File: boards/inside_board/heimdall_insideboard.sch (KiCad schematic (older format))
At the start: 53 parts, among them J1 Barrel_Jack_Switch, J2 Screw_Terminal_01x04, J3 Conn_01x09, J4 Screw_Terminal_01x04, J5 Conn_01x09, J6 Screw_Terminal_01x04, J7 Screw_Terminal_01x06, J8 Screw_Terminal_01x09, J9 Screw_Terminal_01x02, K1 Relay_HJR-3FF-S-Z-5VDC, K2 Relay_HJR-3FF-S-Z-5VDC, K3 Relay_HJR-3FF-S-Z-5VDC, Q1 2N3904, Q2 2N3904, Q3 2N3904, Q4 2N3904, Q5 2N3904, U1 LM1117-3.3, U2 L7805, U3 ESP32_Dev_Board_30Pin

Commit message: update the inside board PCB design file
a number of changes:

 - add an extra terminal to the wiegand header for the 26/34 mode
   switching pin that most wiegand readers have, complete with a
   jumper to selectively connect that terminal to ground
 - expand screw terminal silkscreen outline to fit the actual size
   of the screw terminals; i misread the datasheet when laying them
   out in the previous board revision
 - move the 5v regulator .2" to the right so that there's more
   clearance between it and the 3.3v one when the heatsinks are
   attached
 - correspondingly, move the ESP32 left by about .1" to make room
   for the tamper switch screw terminal's actual size
 - move neighboring resistors closer since they fit well within
   their component outline
 - change the transistor footprint to one with wider spacing, for
   ease of soldering by volunteers
 - add labels for the 12v plug and the fuse that can still be seen
   once the components are installed
 - add a through-hole addressable RGB LED for board status
   signalling and other shenanigans
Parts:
- added D4: NeoPixel_THT, LED_THT:LED_D5.0mm-4_RGB_Wide_Pins, symbol LED:NeoPixel_THT
- added JP4: Jumper, Connector_PinHeader_2.54mm:PinHeader_1x02_P2.54mm_Vertical, symbol Jumper:Jumper_2_Open
- J7: footprint Javawizard_Common_Footprints:PinHeader_JW_1x06_P5.00mm_Vertical -> Javawizard_Common_Footprints:PinHeader_JW_1x07_P5.00mm_Vertical; symbol Connector:Screw_Terminal_01x06 -> Connector:Screw_Terminal_01x07
- K1, K2, K3: symbol Javawizard_Common_Schematic_Symbols:Relay_HJR-3FF-S-Z-5VDC -> heimdall_insideboard-rescue:Relay_HJR-3FF-S-Z-5VDC-Javawizard_Common_Schematic_Symbols
- Q1, Q2, Q3, Q4, Q5: footprint Package_TO_SOT_THT:TO-92_Inline -> Package_TO_SOT_THT:TO-92_Inline_Wide
- U3: symbol Javawizard_Common_Schematic_Symbols:ESP32_Dev_Board_30Pin -> heimdall_insideboard-rescue:ESP32_Dev_Board_30Pin-Javawizard_Common_Schematic_Symbols
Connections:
- net +12V: now also J7.7 (Pin_7); no longer J7.6 (Pin_6)
- net +5V: now also D4.3 (VDD)
- net GND: now also J2.1 (Pin_1), J4.1 (Pin_1), J6.1 (Pin_1), J7.6 (Pin_6), D4.2 (GND), JP4.1 (A); no longer J2.4 (Pin_4), J4.4 (Pin_4), J6.4 (Pin_4), J7.5 (Pin_5)
- net RELAY1_C: now also J2.3 (Pin_3); no longer J2.2 (Pin_2)
- net RELAY1_NC: now also J2.4 (Pin_4); no longer J2.1 (Pin_1)
- net RELAY1_NO: now also J2.2 (Pin_2); no longer J2.3 (Pin_3)
- net RELAY2_C: now also J4.3 (Pin_3); no longer J4.2 (Pin_2)
- net RELAY2_NC: now also J4.4 (Pin_4); no longer J4.1 (Pin_1)
- net RELAY2_NO: now also J4.2 (Pin_2); no longer J4.3 (Pin_3)
- net RELAY3_C: now also J6.3 (Pin_3); no longer J6.2 (Pin_2)
- net RELAY3_NC: now also J6.4 (Pin_4); no longer J6.1 (Pin_1)
- net RELAY3_NO: now also J6.2 (Pin_2); no longer J6.3 (Pin_3)
- net at U3.18 (IO15_PWM): now also D4.4 (DIN)
- new net: J7.5 (Pin_5), JP4.2 (B)
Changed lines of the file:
@@
 $EndComp
 $Comp
-L Javawizard_Common_Schematic_Symbols:ESP32_Dev_Board_30Pin U3
+L heimdall_insideboard-rescue:ESP32_Dev_Board_30Pin-Javawizard_Common_Schematic_Symbols U3
 U 1 1 5F0E43E4
 P 5200 3000
@@
 	4350 4550 4400 4550
 $Comp
-L Javawizard_Common_Schematic_Symbols:Relay_HJR-3FF-S-Z-5VDC K1
+L heimdall_insideboard-rescue:Relay_HJR-3FF-S-Z-5VDC-Javawizard_Common_Schematic_Symbols K1
 U 1 1 5F0E96C1
 P 8800 650
@@
 F 0 "Q1" H 8640 1846 50  0000 L CNN
 F 1 "2N3904" H 8640 1755 50  0000 L CNN
-F 2 "Package_TO_SOT_THT:TO-92_Inline" H 8650 1725 50  0001 L CIN
+F 2 "Package_TO_SOT_THT:TO-92_Inline_Wide" H 8650 1725 50  0001 L CIN
 F 3 "https://www.fairchildsemi.com/datasheets/2N/2N3904.pdf" H 8450 1800 50  0001 L CNN
 	1    8450 1800
@@
 L Connector:Screw_Terminal_01x04 J2
 U 1 1 5F123CCA
-P 10200 1900
-F 0 "J2" H 10280 1892 50  0000 L CNN
-F 1 "Screw_Terminal_01x04" H 10280 1801 50  0000 L CNN
-F 2 "Javawizard_Common_Footprints:PinHeader_JW_1x04_P5.00mm_Vertical" H 10200 1900 50  0001 C CNN
-F 3 "~" H 10200 1900 50  0001 C CNN
-	1    10200 1900
-	1    0    0    -1
+P 10200 2000
+F 0 "J2" H 10280 1992 50  0000 L CNN
+F 1 "Screw_Terminal_01x04" H 10280 1901 50  0000 L CNN
+F 2 "Javawizard_Common_Footprints:PinHeader_JW_1x04_P5.00mm_Vertical" H 10200 2000 50  0001 C CNN
+F 3 "~" H 10200 2000 50  0001 C CNN
+	1    10200 2000
+	1    0    0    1
 $EndComp
 Wire Wire Line
@@
 	7450 4050 7450 3700
 $Comp
-L Javawizard_Common_Schematic_Symbols:Relay_HJR-3FF-S-Z-5VDC K2
+L heimdall_insideboard-rescue:Relay_HJR-3FF-S-Z-5VDC-Javawizard_Common_Schematic_Symbols K2
 U 1 1 5F14E304
 P 8800 2550
@@
 F 0 "Q2" H 8640 3746 50  0000 L CNN
 F 1 "2N3904" H 8640 3655 50  0000 L CNN
-F 2 "Package_TO_SOT_THT:TO-92_Inline" H 8650 3625 50  0001 L CIN
+F 2 "Package_TO_SOT_THT:TO-92_Inline_Wide" H 8650 3625 50  0001 L CIN
 F 3 "https://www.fairchildsemi.com/datasheets/2N/2N3904.pdf" H 8450 3700 50  0001 L CNN
 	1    8450 3700
@@
 L Connector:Screw_Terminal_01x04 J4
 U 1 1 5F14E335
-P 10200 3800
-F 0 "J4" H 10280 3792 50  0000 L CNN
-F 1 "Screw_Terminal_01x04" H 10280 3701 50  0000 L CNN
-F 2 "Javawizard_Common_Footprints:PinHeader_JW_1x04_P5.00mm_Vertical" H 10200 3800 50  0001 C CNN
-F 3 "~" H 10200 3800 50  0001 C CNN
-	1    10200 3800
-	1    0    0    -1
+P 10200 3900
+F 0 "J4" H 10280 3892 50  0000 L CNN
+F 1 "Screw_Terminal_01x04" H 10280 3801 50  0000 L CNN
+F 2 "Javawizard_Common_Footprints:PinHeader_JW_1x04_P5.00mm_Vertical" H 10200 3900 50  0001 C CNN
+F 3 "~" H 10200 3900 50  0001 C CNN
+	1    10200 3900
+	1    0    0    1
 $EndComp
 Wire Wire Line
@@
 	10500 2750 10500 2850
 $Comp
-L Javawizard_Common_Schematic_Symbols:Relay_HJR-3FF-S-Z-5VDC K3
+L heimdall_insideboard-rescue:Relay_HJR-3FF-S-Z-5VDC-Javawizard_Common_Schematic_Symbols K3
 U 1 1 5F1565E6
 P 8800 4450
@@
 F 0 "Q3" H 8640 5646 50  0000 L CNN
 F 1 "2N3904" H 8640 5555 50  0000 L CNN
-F 2 "Package_TO_SOT_THT:TO-92_Inline" H 8650 5525 50  0001 L CIN
+F 2 "Package_TO_SOT_THT:TO-92_Inline_Wide" H 8650 5525 50  0001 L CIN
 F 3 "https://www.fairchildsemi.com/datasheets/2N/2N3904.pdf" H 8450 5600 50  0001 L CNN
 	1    8450 5600
@@
 L Connector:Screw_Terminal_01x04 J6
 U 1 1 5F156617
-P 10200 5700
-F 0 "J6" H 10280 5692 50  0000 L CNN
-F 1 "Screw_Terminal_01x04" H 10280 5601 50  0000 L CNN
-F 2 "Javawizard_Common_Footprints:PinHeader_JW_1x04_P5.00mm_Vertical" H 10200 5700 50  0001 C CNN
-F 3 "~" H 10200 5700 50  0001 C CNN
-	1    10200 5700
-	1    0    0    -1
+P 10200 5800
+F 0 "J6" H 10280 5792 50  0000 L CNN
+F 1 "Screw_Terminal_01x04" H 10280 5701 50  0000 L CNN
+F 2 "Javawizard_Common_Footprints:PinHeader_JW_1x04_P5.00mm_Vertical" H 10200 5800 50  0001 C CNN
+F 3 "~" H 10200 5800 50  0001 C CNN
+	1    10200 5800
+	1    0    0    1
 $EndComp
 Wire Wire Line
@@
 	4100 3650 4400 3650
 $Comp
-L Connector:Screw_Terminal_01x06 J7
+L Connector:Screw_Terminal_01x07 J7
 U 1 1 5F2A191F
-P 1250 6150
-F 0 "J7" H 1168 5625 50  0000 C CNN
-F 1 "Screw_Terminal_01x06" H 1168 5716 50  0000 C CNN
-F 2 "Javawizard_Common_Footprints:PinHeader_JW_1x06_P5.00mm_Vertical" H 1250 6150 50  0001 C CNN
-F 3 "~" H 1250 6150 50  0001 C CNN
-	1    1250 6150
+P 1250 6050
+F 0 "J7" H 1168 5525 50  0000 C CNN
+F 1 "Screw_Terminal_01x06" H 1168 5616 50  0000 C CNN
+F 2 "Javawizard_Common_Footprints:PinHeader_JW_1x07_P5.00mm_Vertical" H 1250 6050 50  0001 C CNN
+F 3 "~" H 1250 6050 50  0001 C CNN
+	1    1250 6050
 	-1   0    0    1
 $EndComp
@@
 L power:+12V #PWR022
 U 1 1 5F2A5516
-P 2000 5650
-F 0 "#PWR022" H 2000 5500 50  0001 C CNN
-F 1 "+12V" H 2015 5823 50  0000 C CNN
-F 2 "" H 2000 5650 50  0001 C CNN
-F 3 "" H 2000 5650 50  0001 C CNN
-	1    2000 5650
-	1    0    0    -1
-$EndComp
-Wire Wire Line
-	2000 5850 1450 5850
+P 2000 5550
+F 0 "#PWR022" H 2000 5400 50  0001 C CNN
+F 1 "+12V" H 2015 5723 50  0000 C CNN
+F 2 "" H 2000 5550 50  0001 C CNN
+F 3 "" H 2000 5550 50  0001 C CNN
+	1    2000 5550
+	1    0    0    -1
+$EndComp
+Wire Wire Line
+	2000 5750 1450 5750
 $Comp
 L power:GND #PWR028
 U 1 1 5F2ADB21
-P 2000 6650
-F 0 "#PWR028" H 2000 6400 50  0001 C CNN
-F 1 "GND" H 2005 6477 50  0000 C CNN
-F 2 "" H 2000 6650 50  0001 C CNN
-F 3 "" H 2000 6650 50  0001 C CNN
-	1    2000 6650
-	1    0    0    -1
-$EndComp
-Wire Wire Line
-	2000 6650 2000 5950
-Wire Wire Line
-	2000 5950 1450 5950
+P 2000 7200
+F 0 "#PWR028" H 2000 6950 50  0001 C CNN
+F 1 "GND" H 2005 7027 50  0000 C CNN
+F 2 "" H 2000 7200 50  0001 C CNN
+F 3 "" H 2000 7200 50  0001 C CNN
+	1    2000 7200
+	1    0    0    -1
+$EndComp
+Wire Wire Line
+	2000 5850 1450 5850
 $Comp
 L Device:R_Small_US R16
@@
 $EndComp
 Wire Wire Line
-	2000 5850 2000 5650
+	2000 5750 2000 5550
 $Comp
 L Device:R_Small_US R22
@@
 F 0 "Q4" H 4140 7096 50  0000 L CNN
 F 1 "2N3904" H 4140 7005 50  0000 L CNN
-F 2 "Package_TO_SOT_THT:TO-92_Inline" H 4150 6975 50  0001 L CIN
+F 2 "Package_TO_SOT_THT:TO-92_Inline_Wide" H 4150 6975 50  0001 L CIN
 F 3 "https://www.fairchildsemi.com/datasheets/2N/2N3904.pdf" H 3950 7050 50  0001 L CNN
 	1    3950 7050
@@
 F 0 "Q5" H 4990 7096 50  0000 L CNN
 F 1 "2N3904" H 4990 7005 50  0000 L CNN
-F 2 "Package_TO_SOT_THT:TO-92_Inline" H 5000 6975 50  0001 L CIN
+F 2 "Package_TO_SOT_THT:TO-92_Inline_Wide" H 5000 6975 50  0001 L CIN
 F 3 "https://www.fairchildsemi.com/datasheets/2N/2N3904.pdf" H 4800 7050 50  0001 L CNN
 	1    4800 7050
@@
 Wire Wire Line
 	7000 3750 6000 3750
+$Comp
+L LED:NeoPixel_THT D4
+U 1 1 6058485B
+P 5350 5450
+F 0 "D4" H 5694 5496 50  0000 L CNN
+F 1 "NeoPixel_THT" H 5694 5405 50  0000 L CNN
+F 2 "LED_THT:LED_D5.0mm-4_RGB_Wide_Pins" H 5400 5150 50  0001 L TNN
+F 3 "https://www.adafruit.com/product/1938" H 5450 5075 50  0001 L TNN
+	1    5350 5450
+	1    0    0    -1
+$EndComp
+$Comp
+L power:+5V #PWR0104
+U 1 1 605868AC
+P 5350 5050
+F 0 "#PWR0104" H 5350 4900 50  0001 C CNN
+F 1 "+5V" H 5365 5223 50  0000 C CNN
+F 2 "" H 5350 5050 50  0001 C CNN
+F 3 "" H 5350 5050 50  0001 C CNN
+	1    5350 5050
+	1    0    0    -1
+$EndComp
+$Comp
+L power:GND #PWR0105
+U 1 1 605DA8FD
+P 5350 5950
+F 0 "#PWR0105" H 5350 5700 50  0001 C CNN
+F 1 "GND" H 5355 5777 50  0000 C CNN
+F 2 "" H 5350 5950 50  0001 C CNN
+F 3 "" H 5350 5950 50  0001 C CNN
+	1    5350 5950
+	1    0    0    -1
+$EndComp
+Wire Wire Line
+	5350 5050 5350 5150
+Wire Wire Line
+	5350 5750 5350 5950
+Wire Wire Line
+	6000 4350 6500 4350
+Wire Wire Line
+	6500 4350 6500 4800
+Wire Wire Line
+	6500 4800 4750 4800
+Wire Wire Line
+	4750 4800 4750 5450
+Wire Wire Line
+	4750 5450 5050 5450
+$Comp
+L Jumper:Jumper_2_Open JP4
+U 1 1 60618C40
+P 1600 6800
+F 0 "JP4" V 1646 6712 50  0000 R CNN
+F 1 "Jumper" V 1555 6712 50  0000 R CNN
+F 2 "Connector_PinHeader_2.54mm:PinHeader_1x02_P2.54mm_Vertical" H 1600 6800 50  0001 C CNN
+F 3 "~" H 1600 6800 50  0001 C CNN
+	1    1600 6800
+	0    -1   -1   0
+$EndComp
+Wire Wire Line
+	2000 5850 2000 7000
+Wire Wire Line
+	1600 6600 1600 5950
+Wire Wire Line
+	1600 5950 1450 5950
+Wire Wire Line
+	1600 7000 2000 7000
+Connection ~ 2000 7000
+Wire Wire Line
+	2000 7000 2000 7200
 $EndSCHEMATC

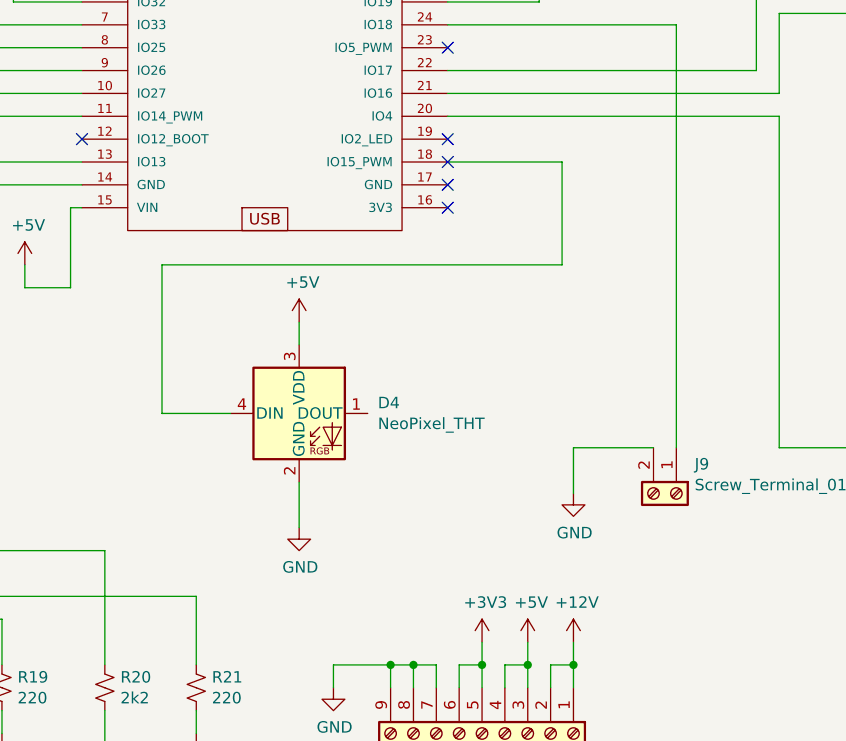
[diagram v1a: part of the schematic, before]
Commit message: inside board version 3
- add a 3.3v -> 5v level shifting circuit to the addressable RGB
  LED's input. it seems to work without it in my testing of board
  version 2, but I'd rather not find out the hard way that it works
  for some LEDs but not for others since it's out of spec for what
  they're supposed to require, which is 0.7*VCC = 3.5v for logic
  level high signals.
- a handful of vias were underneath where the voltage regulator
  heat sinks go. to prevent the heatsinks from coming in contact
  with them, move them outside of the heat sinks' footprint.
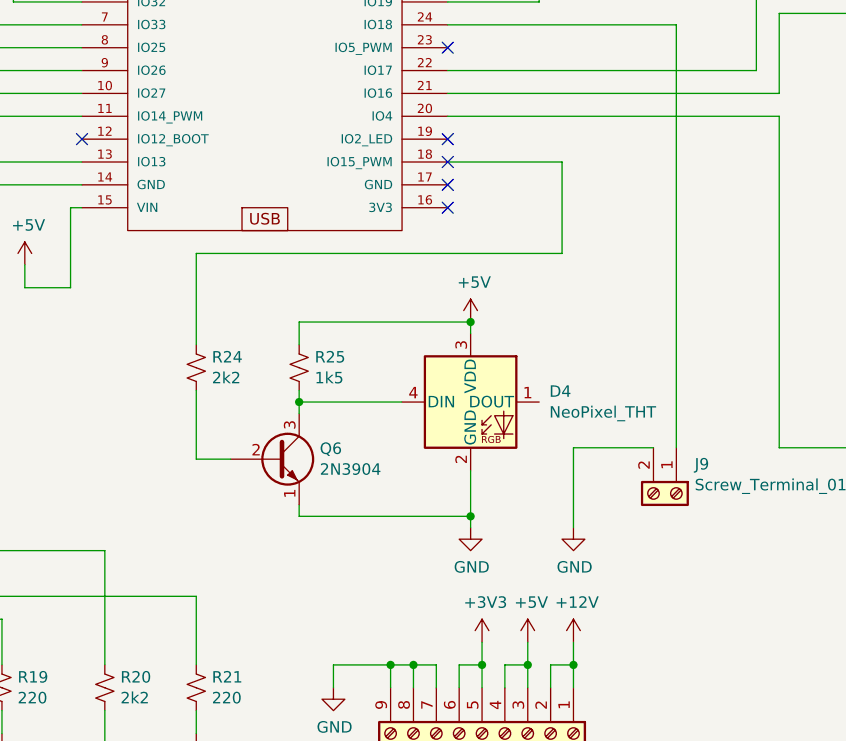
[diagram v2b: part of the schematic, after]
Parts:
- added Q6: 2N3904, Package_TO_SOT_THT:TO-92_Inline_Wide, symbol Transistor_BJT:2N3904
- added R24: 2k2, Resistor_THT:R_Axial_DIN0207_L6.3mm_D2.5mm_P10.16mm_Horizontal, symbol Device:R_Small_US
- added R25: 1k5, Resistor_THT:R_Axial_DIN0207_L6.3mm_D2.5mm_P10.16mm_Horizontal, symbol Device:R_Small_US
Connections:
- net +5V: now also R25.1
- net GND: now also Q6.1 (E)
- net at U3.18 (IO15_PWM): now also R24.1; no longer D4.4 (DIN)
- new net: D4.4 (DIN), Q6.3 (C), R25.2
- new net: Q6.2 (B), R24.2
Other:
- moved on the sheet: D4
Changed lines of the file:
@@
 L power:GND #PWR0103
 U 1 1 5F140007
-P 6550 5800
-F 0 "#PWR0103" H 6550 5550 50  0001 C CNN
-F 1 "GND" H 6555 5627 50  0000 C CNN
-F 2 "" H 6550 5800 50  0001 C CNN
-F 3 "" H 6550 5800 50  0001 C CNN
-	1    6550 5800
+P 6550 5950
+F 0 "#PWR0103" H 6550 5700 50  0001 C CNN
+F 1 "GND" H 6555 5777 50  0000 C CNN
+F 2 "" H 6550 5950 50  0001 C CNN
+F 3 "" H 6550 5950 50  0001 C CNN
+	1    6550 5950
 	1    0    0    -1
 $EndComp
 Wire Wire Line
 	6900 5600 6550 5600
-Wire Wire Line
-	6550 5600 6550 5800
 Wire Wire Line
 	7000 5600 7000 3750
@@
 L LED:NeoPixel_THT D4
 U 1 1 6058485B
-P 5350 5450
-F 0 "D4" H 5694 5496 50  0000 L CNN
-F 1 "NeoPixel_THT" H 5694 5405 50  0000 L CNN
-F 2 "LED_THT:LED_D5.0mm-4_RGB_Wide_Pins" H 5400 5150 50  0001 L TNN
-F 3 "https://www.adafruit.com/product/1938" H 5450 5075 50  0001 L TNN
-	1    5350 5450
+P 6100 5400
+F 0 "D4" H 6444 5446 50  0000 L CNN
+F 1 "NeoPixel_THT" H 6444 5355 50  0000 L CNN
+F 2 "LED_THT:LED_D5.0mm-4_RGB_Wide_Pins" H 6150 5100 50  0001 L TNN
+F 3 "https://www.adafruit.com/product/1938" H 6200 5025 50  0001 L TNN
+	1    6100 5400
 	1    0    0    -1
 $EndComp
@@
 L power:+5V #PWR0104
 U 1 1 605868AC
-P 5350 5050
-F 0 "#PWR0104" H 5350 4900 50  0001 C CNN
-F 1 "+5V" H 5365 5223 50  0000 C CNN
-F 2 "" H 5350 5050 50  0001 C CNN
-F 3 "" H 5350 5050 50  0001 C CNN
-	1    5350 5050
+P 6100 5050
+F 0 "#PWR0104" H 6100 4900 50  0001 C CNN
+F 1 "+5V" H 6115 5223 50  0000 C CNN
+F 2 "" H 6100 5050 50  0001 C CNN
+F 3 "" H 6100 5050 50  0001 C CNN
+	1    6100 5050
 	1    0    0    -1
 $EndComp
@@
 L power:GND #PWR0105
 U 1 1 605DA8FD
-P 5350 5950
-F 0 "#PWR0105" H 5350 5700 50  0001 C CNN
-F 1 "GND" H 5355 5777 50  0000 C CNN
-F 2 "" H 5350 5950 50  0001 C CNN
-F 3 "" H 5350 5950 50  0001 C CNN
-	1    5350 5950
+P 6100 5950
+F 0 "#PWR0105" H 6100 5700 50  0001 C CNN
+F 1 "GND" H 6105 5777 50  0000 C CNN
+F 2 "" H 6100 5950 50  0001 C CNN
+F 3 "" H 6100 5950 50  0001 C CNN
+	1    6100 5950
 	1    0    0    -1
 $EndComp
 Wire Wire Line
-	5350 5050 5350 5150
-Wire Wire Line
-	5350 5750 5350 5950
-Wire Wire Line
 	6000 4350 6500 4350
-Wire Wire Line
-	6500 4350 6500 4800
-Wire Wire Line
-	6500 4800 4750 4800
-Wire Wire Line
-	4750 4800 4750 5450
-Wire Wire Line
-	4750 5450 5050 5450
 $Comp
 L Jumper:Jumper_2_Open JP4
@@
 Wire Wire Line
 	2000 7000 2000 7200
+Wire Wire Line
+	6100 5100 6100 5050
+$Comp
+L Transistor_BJT:2N3904 Q6
+U 1 1 607CCCEB
+P 5250 5650
+F 0 "Q6" H 5440 5696 50  0000 L CNN
+F 1 "2N3904" H 5440 5605 50  0000 L CNN
+F 2 "Package_TO_SOT_THT:TO-92_Inline_Wide" H 5450 5575 50  0001 L CIN
+F 3 "https://www.fairchildsemi.com/datasheets/2N/2N3904.pdf" H 5250 5650 50  0001 L CNN
+	1    5250 5650
+	1    0    0    -1
+$EndComp
+$Comp
+L Device:R_Small_US R25
+U 1 1 607CE114
+P 5350 5250
+F 0 "R25" H 5418 5296 50  0000 L CNN
+F 1 "1k5" H 5418 5205 50  0000 L CNN
+F 2 "Resistor_THT:R_Axial_DIN0207_L6.3mm_D2.5mm_P10.16mm_Horizontal" H 5350 5250 50  0001 C CNN
+F 3 "~" H 5350 5250 50  0001 C CNN
+	1    5350 5250
+	1    0    0    -1
+$EndComp
+Wire Wire Line
+	6100 5050 5350 5050
+Wire Wire Line
+	5350 5050 5350 5150
+Connection ~ 6100 5050
+Wire Wire Line
+	5350 5350 5350 5400
+Wire Wire Line
+	6550 5600 6550 5950
+Wire Wire Line
+	6100 5700 6100 5900
+Wire Wire Line
+	5350 5850 5350 5900
+Wire Wire Line
+	5350 5900 6100 5900
+Connection ~ 6100 5900
+Wire Wire Line
+	6100 5900 6100 5950
+Wire Wire Line
+	5800 5400 5350 5400
+Connection ~ 5350 5400
+Wire Wire Line
+	5350 5400 5350 5450
+$Comp
+L Device:R_Small_US R24
+U 1 1 60858559
+P 4900 5250
+F 0 "R24" H 4968 5296 50  0000 L CNN
+F 1 "2k2" H 4968 5205 50  0000 L CNN
+F 2 "Resistor_THT:R_Axial_DIN0207_L6.3mm_D2.5mm_P10.16mm_Horizontal" H 4900 5250 50  0001 C CNN
+F 3 "~" H 4900 5250 50  0001 C CNN
+	1    4900 5250
+	1    0    0    -1
+$EndComp
+Wire Wire Line
+	4900 5350 4900 5650
+Wire Wire Line
+	4900 5650 5050 5650
+Wire Wire Line
+	4900 5150 4900 4750
+Wire Wire Line
+	4900 4750 6500 4750
+Wire Wire Line
+	6500 4750 6500 4350
 $EndSCHEMATC
